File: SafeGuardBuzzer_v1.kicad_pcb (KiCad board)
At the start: 2 copper layers, 90 x 45 mm, 16 parts, among them J1 SWD_DEBUG, J2 VBAT_GND_TEST, Q1 AO3400A, U1 DA14531MOD-00F01002

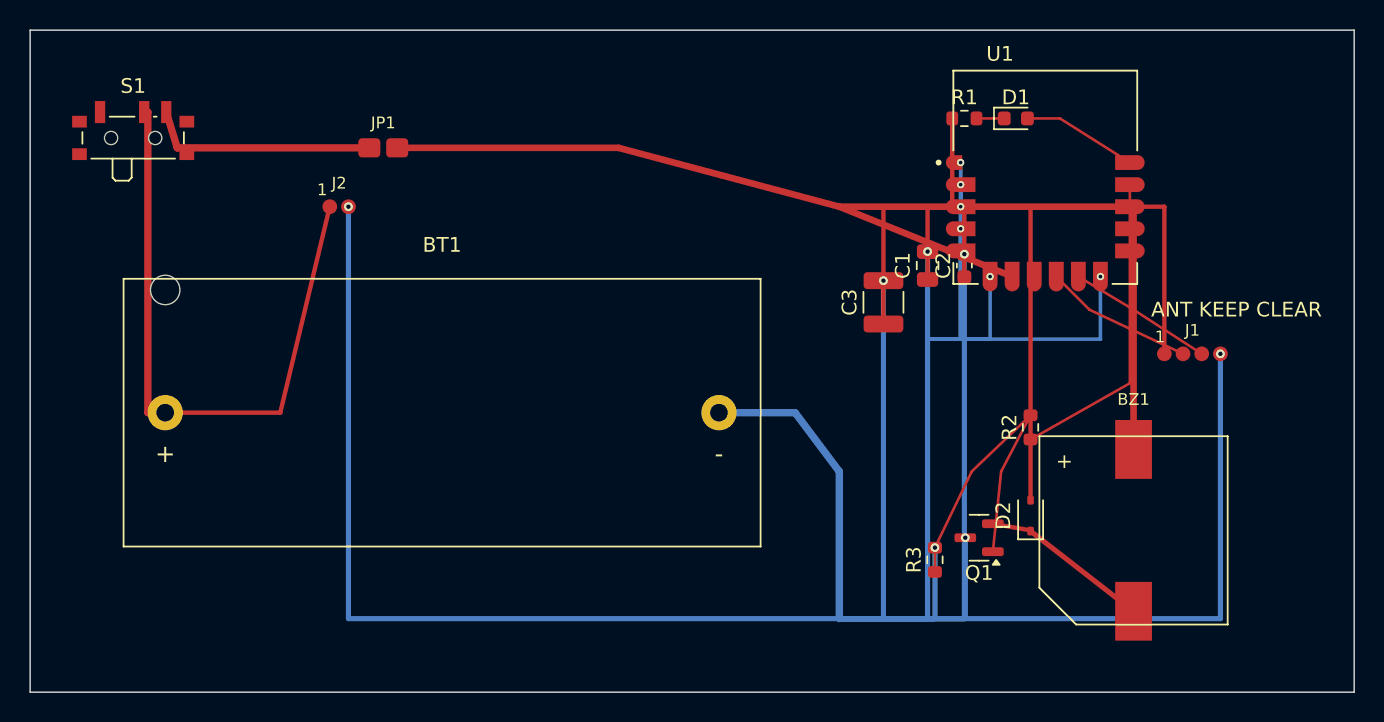
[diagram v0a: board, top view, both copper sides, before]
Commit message: Clean Buzzer RF keepout and DRC before routing
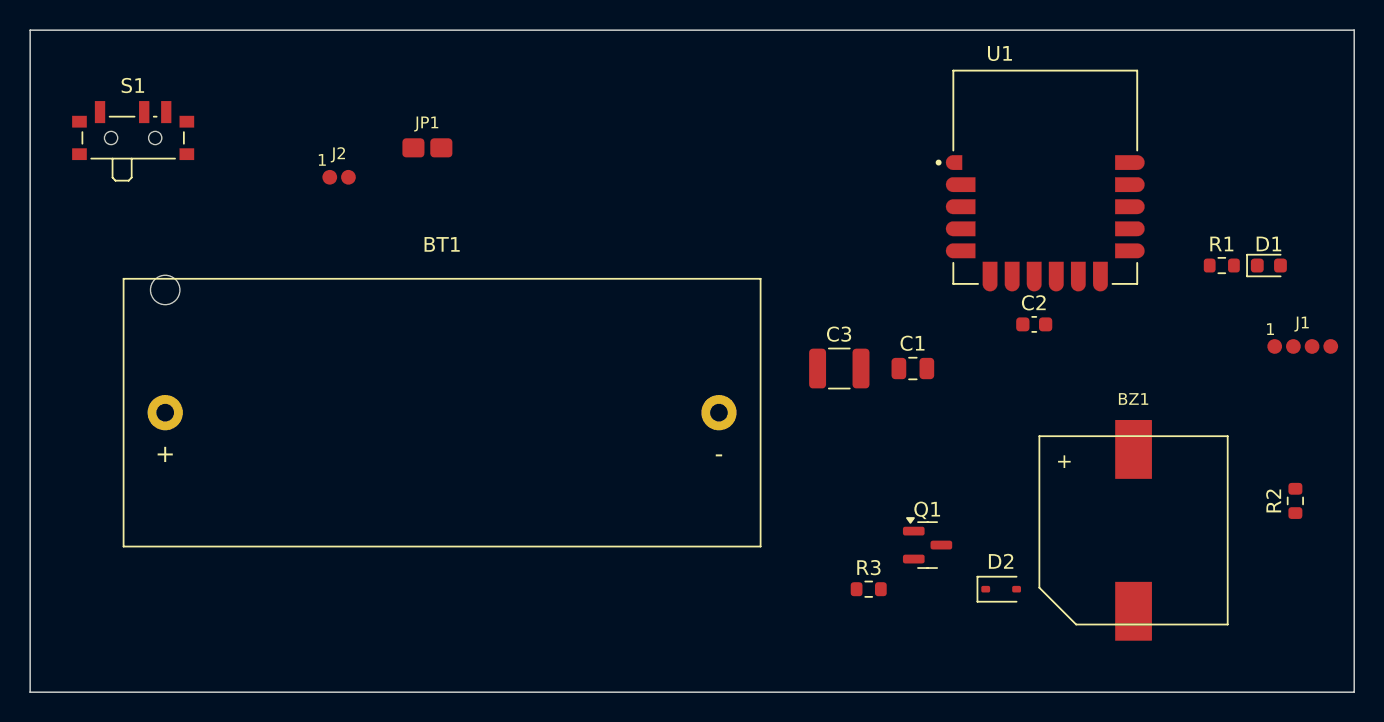
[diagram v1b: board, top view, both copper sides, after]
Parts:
- moved R1 20.2 mm to (81.0, 16.0)
- moved D1 19.9 mm to (84.2, 16.0)
- moved R2 18.7 mm to (86.0, 32.0)
- moved J1 7.52 mm to (86.5, 21.5)
- moved C1 7.07 mm to (60.0, 23.0), turned to 0 degrees
- moved C2 6.21 mm to (68.2, 20.0), turned to 0 degrees
- moved C3 5.41 mm to (55.0, 23.0), turned to 0 degrees
- moved D2 5.39 mm to (66.0, 38.0), turned to 0 degrees
- moved R3 4.92 mm to (57.0, 38.0), turned to 0 degrees
- moved Q1 3.54 mm to (61.0, 35.0), turned to 0 degrees
- moved JP1 3.00 mm to (27.0, 8.00)
- moved J2 2.00 mm to (21.0, 10.0)
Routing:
- net GND: track 463.5 -> 0.00 mm, vias 13 -> 0
- net VCC: track 193.7 -> 0.00 mm
- net VBAT_RAW: track 44.1 -> 0.00 mm
- net BUZZER_PWM_GATE: track 22.7 -> 0.00 mm
- net BUZZER_PWM: track 21.3 -> 0.00 mm
- net VBAT_SW: track 15.6 -> 0.00 mm
- net BUZZER_NEG: track 11.5 -> 0.00 mm
- net SWDIO: track 10.2 -> 0.00 mm
- net SWCLK: track 9.89 -> 0.00 mm
- net LED_STATUS: track 7.83 -> 0.00 mm
- net LED_A: track 1.89 -> 0.00 mm

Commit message: Route initial Buzzer power path
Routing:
- net GND: track 0.00 -> 99.7 mm, vias 0 -> 5
- net VBAT_RAW: track 0.00 -> 63.7 mm
- net VCC: track 0.00 -> 45.2 mm, vias 0 -> 2
- net VBAT_SW: track 0.00 -> 21.9 mm

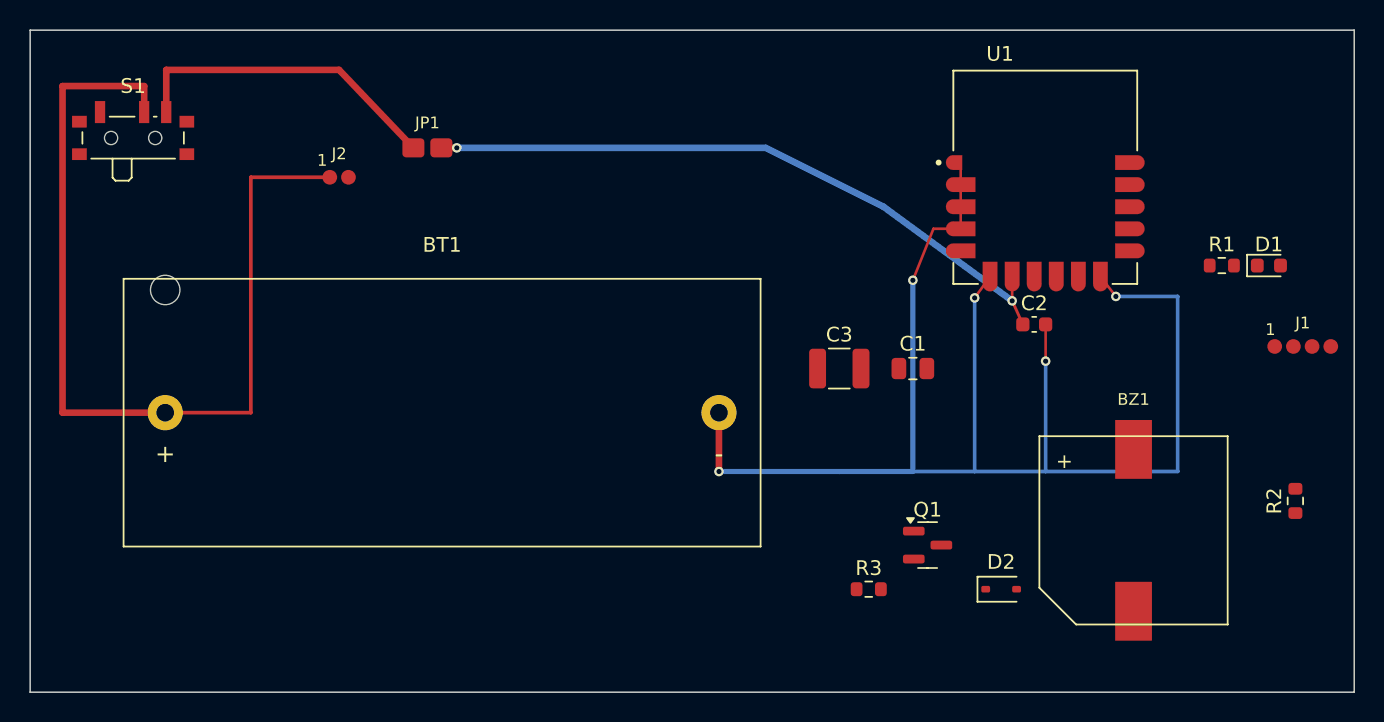
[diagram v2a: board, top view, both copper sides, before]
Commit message: Complete Buzzer v1 routing
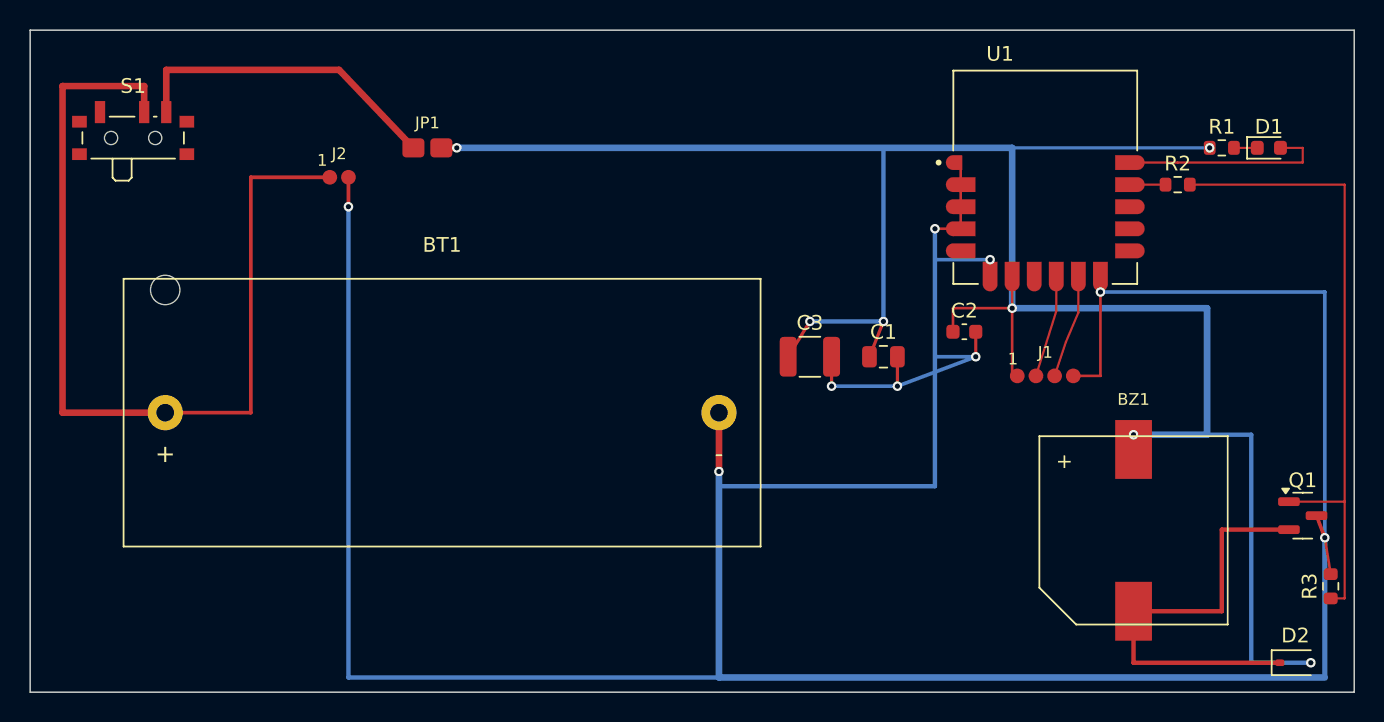
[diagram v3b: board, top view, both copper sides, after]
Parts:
- moved R3 31.4 mm to (88.4, 37.8), turned to 90 degrees
- moved Q1 25.6 mm to (86.5, 33.0)
- moved R2 22.9 mm to (78.0, 10.5), turned to 0 degrees
- moved D2 20.6 mm to (86.0, 43.0)
- moved J1 17.6 mm to (69.0, 23.5)
- moved D1 8.00 mm to (84.2, 8.00)
- moved R1 8.00 mm to (81.0, 8.00)
- moved C2 4.78 mm to (63.5, 20.5)
- moved C1 2.15 mm to (58.0, 22.2)
- moved C3 2.15 mm to (53.0, 22.2)
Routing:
- net GND: track 99.7 -> 244.0 mm, vias 5 -> 9
- net VCC: track 45.2 -> 153.4 mm, vias 2 -> 7
- net BUZZER_PWM_GATE: track 0.00 -> 43.4 mm
- net BUZZER_NEG: track 0.00 -> 29.6 mm
- net LED_STATUS: track 0.00 -> 14.3 mm
- net SWCLK: track 0.00 -> 7.05 mm
- net SWDIO: track 0.00 -> 6.96 mm
- net BUZZER_PWM: track 0.00 -> 2.42 mm
- net LED_A: track 0.00 -> 1.59 mm
